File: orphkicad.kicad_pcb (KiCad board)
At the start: 2 copper layers, 21 x 51 mm, 42 parts, among them J1 USB_C_Receptacle_USB2.0_16P, SW1 BTN_BOOT, SW2 BTN_RST, SW3 BTN_USR, U1 RP2040, U2 W25Q16JVUXIQ, U3 USBLC6-2SC6, U5 XC6206PxxxMR, X1 X322512MSB4SI

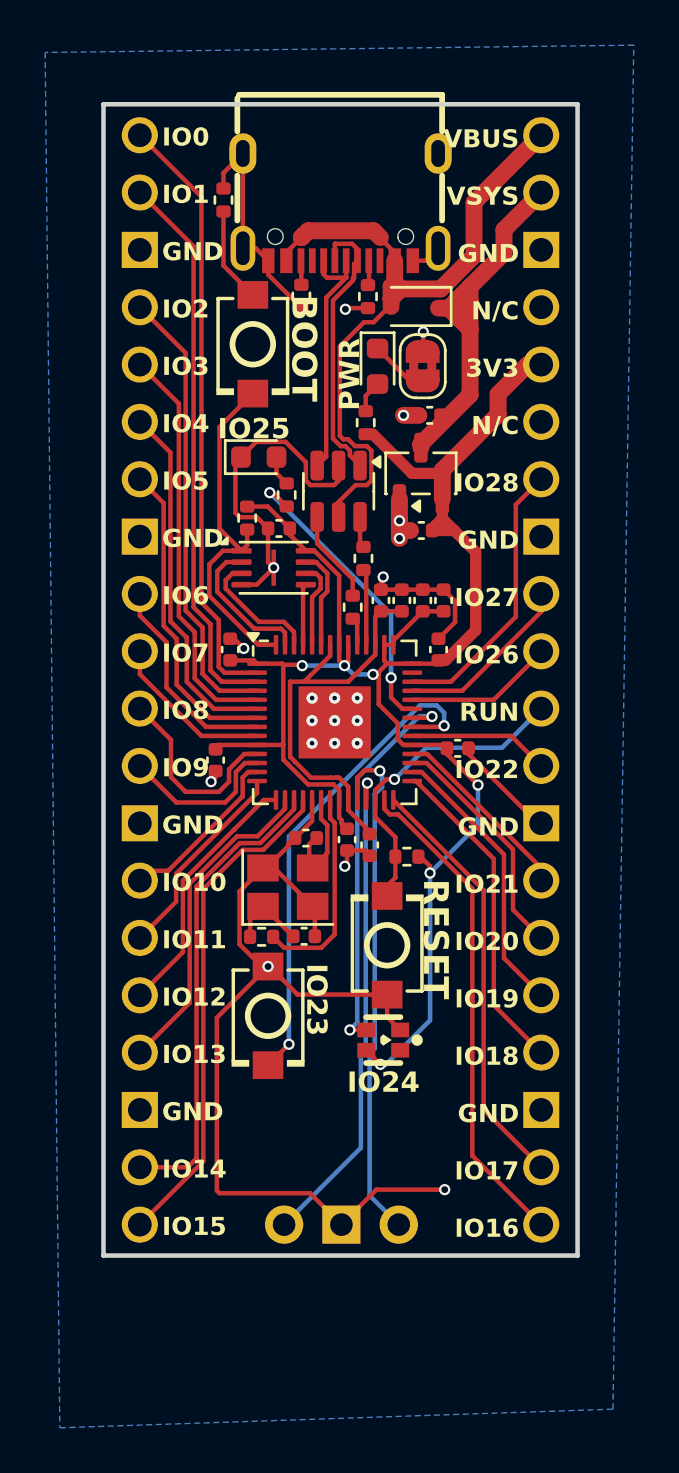
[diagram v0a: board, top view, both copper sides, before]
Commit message: improve routing on esd protection ic
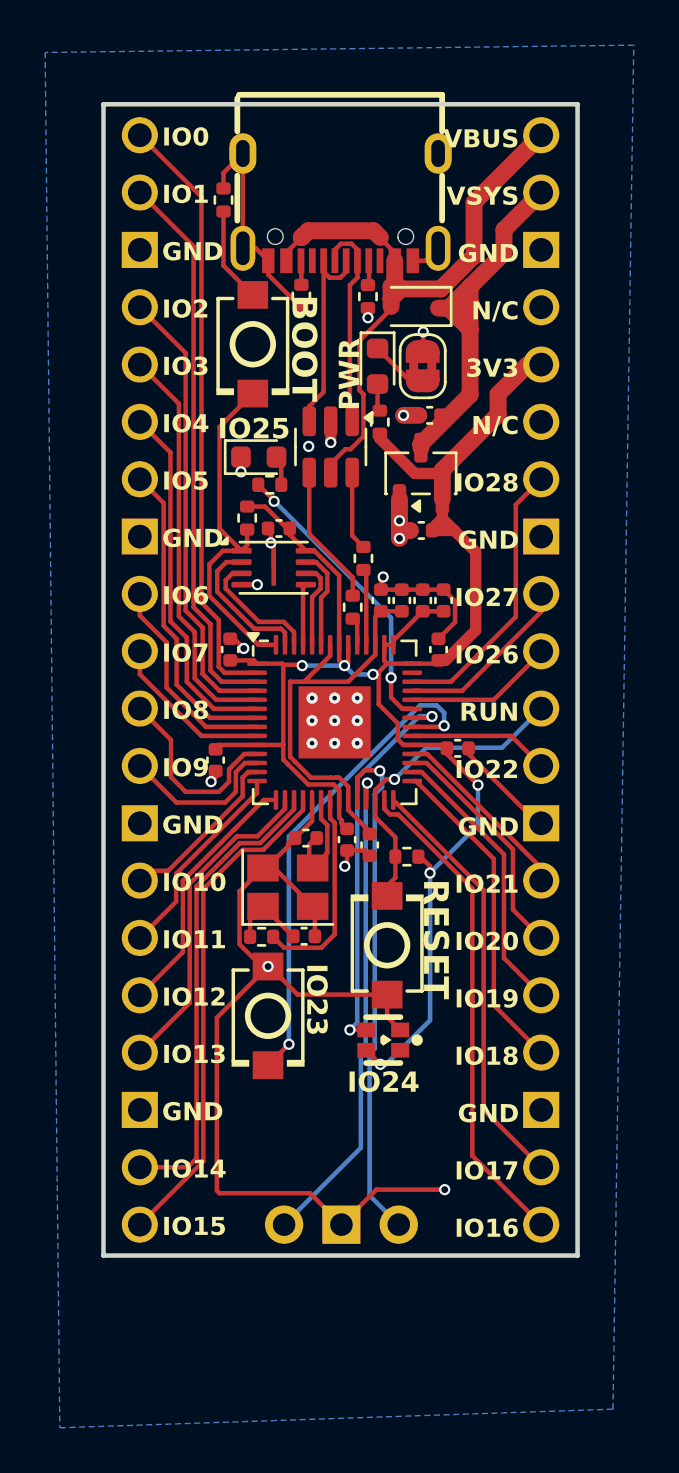
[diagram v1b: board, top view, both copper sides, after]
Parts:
- moved U3 1.99 mm to (80.1, 45.8)
- moved R9 0.87 mm to (77.4, 47.5), turned to 0 degrees
- moved R8 0.63 mm to (82.3, 44.7)
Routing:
- net GND: track 88.4 -> 77.5 mm, vias 21 -> 25
- net VBUS: track 32.4 -> 28.7 mm
- net USB_DM: track 12.5 -> 9.49 mm
- net Net-(R3-Pad1): track 4.14 -> 6.25 mm
- net Net-(R4-Pad1): track 1.39 -> 3.50 mm
- net USB_DP: track 11.3 -> 9.57 mm
